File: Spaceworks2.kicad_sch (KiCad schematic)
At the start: 15 parts, among them J1 IR_CAM, J2 THERMISTOR, J3 STEPPER, U1 DRV8833, U2 ItsyBitsyM4, U3 ITR20001/T

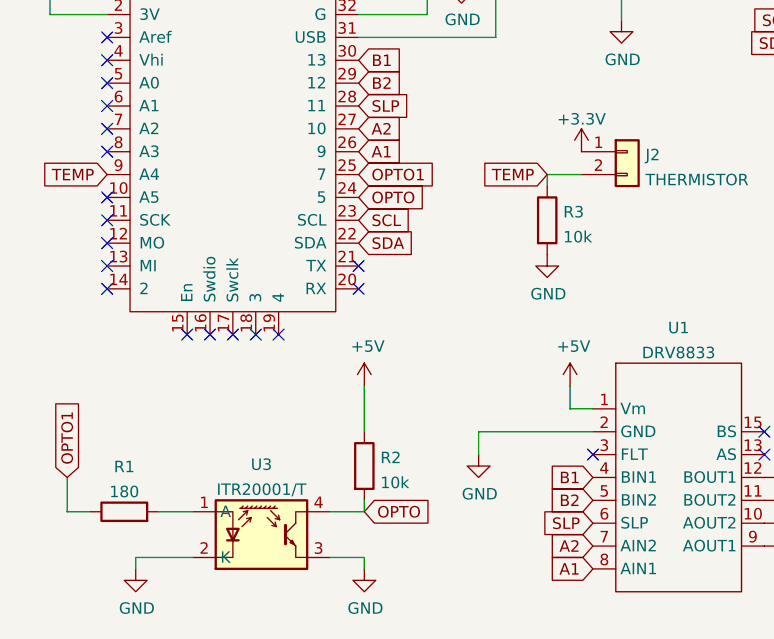
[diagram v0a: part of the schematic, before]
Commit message: Fixed OPTO conn, Thermistor voltage divider resistor
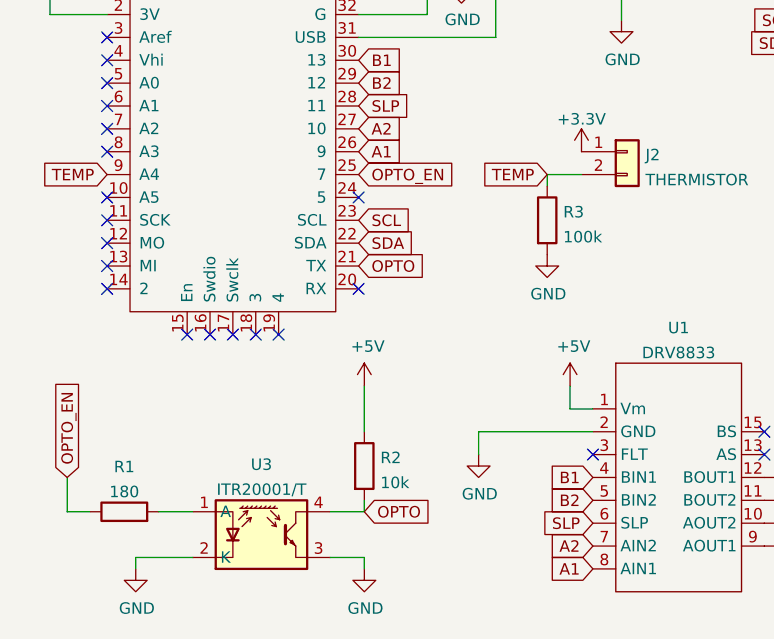
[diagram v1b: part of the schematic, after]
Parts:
- R3: value 10k -> 100k
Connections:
- net OPTO: now also U2.21 (TX); no longer U2.24 (5)
- net OPTO1 renamed OPTO_EN
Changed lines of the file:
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@@
   (no_connect (at 98.425 153.035))
   (no_connect (at 98.425 155.575))
+  (no_connect (at 53.34 127))
   (no_connect (at 53.34 137.16))
-  (no_connect (at 53.34 134.62))
   (no_connect (at 25.4 132.08))
   (no_connect (at 25.4 134.62))
@@
     )
   )
-  (global_label "OPTO1" (shape input) (at 53.34 124.46 0) (fields_autoplaced)
-    (effects (font (size 1.27 1.27)) (justify left))
-    (property "Intersheet References" "${INTERSHEET_REFS}" (id 0) (at 61.7723 124.3806 0)
+  (global_label "OPTO_EN" (shape input) (at 53.34 124.46 0) (fields_autoplaced)
+    (effects (font (size 1.27 1.27)) (justify left))
+    (property "Intersheet References" "${INTERSHEET_REFS}" (id 0) (at 64.0099 124.3806 0)
       (effects (font (size 1.27 1.27)) (justify left) hide)
     )
   )
-  (global_label "OPTO" (shape input) (at 53.34 127 0) (fields_autoplaced)
-    (effects (font (size 1.27 1.27)) (justify left))
-    (property "Intersheet References" "${INTERSHEET_REFS}" (id 0) (at 60.5628 126.9206 0)
+  (global_label "OPTO" (shape input) (at 53.34 134.62 0) (fields_autoplaced)
+    (effects (font (size 1.27 1.27)) (justify left))
+    (property "Intersheet References" "${INTERSHEET_REFS}" (id 0) (at 60.5628 134.5406 0)
       (effects (font (size 1.27 1.27)) (justify left) hide)
     )
@@
     )
   )
-  (global_label "OPTO1" (shape input) (at 20.955 158.115 90) (fields_autoplaced)
-    (effects (font (size 1.27 1.27)) (justify left))
-    (property "Intersheet References" "${INTERSHEET_REFS}" (id 0) (at 20.8756 149.6827 90)
+  (global_label "OPTO_EN" (shape input) (at 20.955 158.115 90) (fields_autoplaced)
+    (effects (font (size 1.27 1.27)) (justify left))
+    (property "Intersheet References" "${INTERSHEET_REFS}" (id 0) (at 20.8756 147.4451 90)
       (effects (font (size 1.27 1.27)) (justify left) hide)
     )
@@
       (effects (font (size 1.27 1.27)) (justify left))
     )
-    (property "Value" "10k" (id 1) (at 76.073 131.4066 0)
+    (property "Value" "100k" (id 1) (at 76.073 131.4066 0)
       (effects (font (size 1.27 1.27)) (justify left))
     )
@@
     )
     (path "/1d3f6624-e5bd-43c5-9fb3-00cc1d807901"
-      (reference "R3") (unit 1) (value "10k") (footprint "Resistor_THT:R_Axial_DIN0207_L6.3mm_D2.5mm_P7.62mm_Horizontal")
+      (reference "R3") (unit 1) (value "100k") (footprint "Resistor_THT:R_Axial_DIN0207_L6.3mm_D2.5mm_P7.62mm_Horizontal")
     )
     (path "/f398c5fb-7b8d-4fdf-b399-85fb98e738d5"
